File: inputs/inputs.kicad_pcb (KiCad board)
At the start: 2 copper layers, 47 x 25.4 mm, 27 parts, among them P1 CONN_01X01, P10 CONN_01X01, P11 CONN_01X01, P12 CONN_01X01, P13 CONN_01X01, P2 CONN_01X01, P3 CONN_01X01, P4 CONN_01X05, P5 CONN_01X01, P6 CONN_01X01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

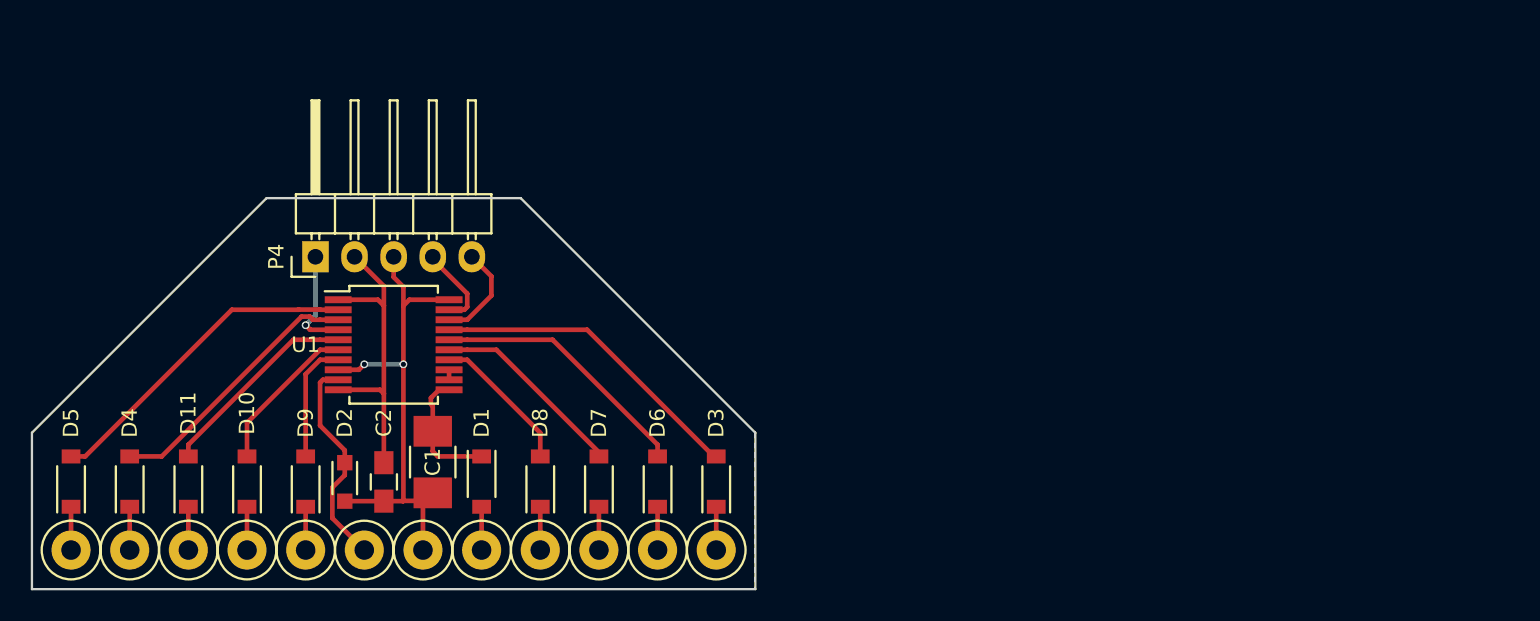
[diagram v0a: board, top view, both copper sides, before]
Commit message: 8 inputs rev 2
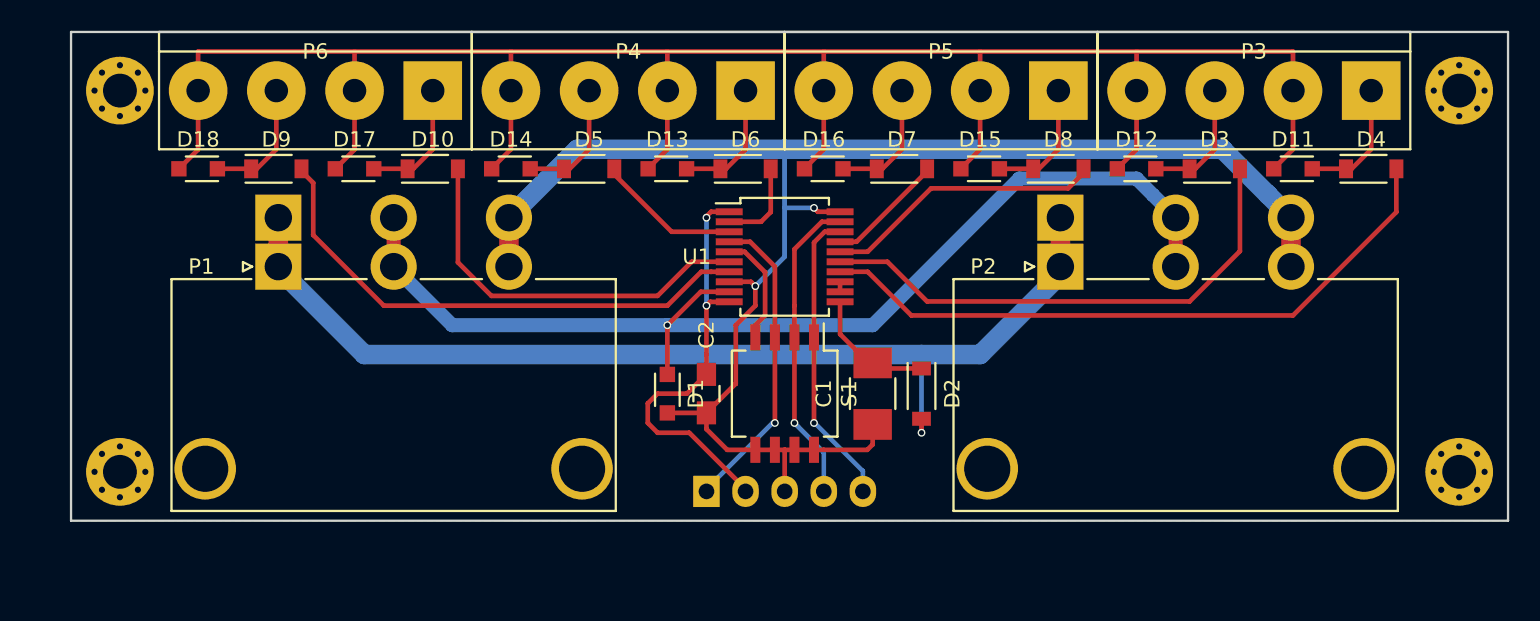
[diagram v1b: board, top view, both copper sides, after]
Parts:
- removed P10, P11, P12, P13, P8, P9: CONN_01X01, footprints:wire_awg_18
- added D12: RSB36V, Diodes_SMD:SOD-323_HandSoldering, F.Cu at (217.8, 64.8)
- added D13: RSB36V, Diodes_SMD:SOD-323_HandSoldering, F.Cu at (187.3, 64.8)
- added D14: RSB36V, Diodes_SMD:SOD-323_HandSoldering, F.Cu at (177.2, 64.8)
- added D15: RSB36V, Diodes_SMD:SOD-323_HandSoldering, F.Cu at (207.6, 64.8)
- added D16: RSB36V, Diodes_SMD:SOD-323_HandSoldering, F.Cu at (197.5, 64.8)
- added D17: RSB36V, Diodes_SMD:SOD-323_HandSoldering, F.Cu at (167.0, 64.8)
- added D18: RSB36V, Diodes_SMD:SOD-323_HandSoldering, F.Cu at (156.8, 64.8)
- added REF**: MountingHole_2.2mm_M2_Pad_Via, Mounting_Holes:MountingHole_2.2mm_M2_Pad_Via, F.Cu at (151.8, 84.5)
- added REF**: MountingHole_2.2mm_M2_Pad_Via, Mounting_Holes:MountingHole_2.2mm_M2_Pad_Via, F.Cu at (151.8, 59.7)
- added REF**: MountingHole_2.2mm_M2_Pad_Via, Mounting_Holes:MountingHole_2.2mm_M2_Pad_Via, F.Cu at (238.8, 59.7)
- added REF**: MountingHole_2.2mm_M2_Pad_Via, Mounting_Holes:MountingHole_2.2mm_M2_Pad_Via, F.Cu at (238.8, 84.5)
- added S1: DIP_SWITCH_4, footprints:Copal_CHS-04TB, F.Cu at (194.9, 79.4)
- D1, D11: value 1N4148W-7-F -> RSB36V; footprint Diodes_SMD:SOD-123 -> Diodes_SMD:SOD-323_HandSoldering
- D2: value RSB36V -> 1N4148W-7-F; footprint Diodes_SMD:SOD-323_HandSoldering -> Diodes_SMD:SOD-123
- P1, P2: value CONN_01X01 -> MOLEX-0431603103; footprint footprints:wire_awg_18 -> Connectors_Molex:Molex_Sabre_43160-XX03_03x7.49mm_Angled_BoardLock
- P3, P5, P6: value CONN_01X01 -> TE-282836-4; footprint footprints:wire_awg_18 -> Connect:bornier4
- P4: value CONN_01X05 -> TE-282836-4; footprint Pin_Headers:Pin_Header_Angled_1x05 -> Connect:bornier4
- P7: value CONN_01X01 -> CONN_01X05; footprint footprints:wire_awg_18 -> Pin_Headers:Pin_Header_Angled_1x05; moved to B.Cu
- moved D4 83.2 mm to (233.0, 64.8), turned to 0 degrees
- moved D11 74.6 mm to (228.0, 64.8), turned to 180 degrees
- moved P3 65.0 mm to (225.4, 59.7), turned to 180 degrees
- moved P2 45.3 mm to (212.9, 71.1)
- moved P7 41.5 mm to (189.9, 85.7), turned to 270 degrees
- moved D5 39.3 mm to (182.2, 64.8), turned to 0 degrees
- moved D8 39.3 mm to (212.7, 64.8), turned to 0 degrees
- moved D3 38.2 mm to (222.9, 64.8), turned to 0 degrees
- moved D2 37.9 mm to (203.8, 79.4)
- moved P5 33.2 mm to (205.1, 59.7), turned to 180 degrees
- moved P6 32.2 mm to (164.5, 59.7), turned to 180 degrees
- moved C1 28.9 mm to (200.7, 79.4)
- moved D7 28.3 mm to (202.6, 64.8), turned to 0 degrees
- moved U1 26.0 mm to (194.9, 70.5)
- moved D10 23.6 mm to (172.1, 64.8), turned to 0 degrees
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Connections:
- net Net-(D10-Pad2) renamed /Sheet584D84B8/CHAN_A
- net Net-(D9-Pad2) renamed /Sheet584D84B8/CHAN_B
- C1 pad 1: +12V -> /Sheet584DA639/+12V
- C2 pad 1: +5V -> /Sheet584DA639/+5V
- D1 pad 1: +12V -> /Sheet584DA639/LBUS
- D1 pad 2: Net-(D1-Pad2) -> GND
- D11 pad 2: Net-(D11-Pad2) -> GND
- D2 pad 1: /LBUS -> /Sheet584DA639/+12V
- D2 pad 2: GND -> /lin_common/12V_UNPROTECTED
- D3 pad 1: Net-(D3-Pad1) -> Net-(D12-Pad1)
- D3 pad 2: Net-(D3-Pad2) -> /Sheet584D6B96/CHAN_B
- D4 pad 1: Net-(D4-Pad1) -> Net-(D11-Pad1)
- D4 pad 2: Net-(D4-Pad2) -> /Sheet584D6B96/CHAN_A
- D5 pad 1: Net-(D5-Pad1) -> Net-(D14-Pad1)
- D5 pad 2: Net-(D5-Pad2) -> /Sheet584D7AB5/CHAN_B
- D6 pad 1: Net-(D6-Pad1) -> Net-(D13-Pad1)
- D6 pad 2: Net-(D6-Pad2) -> /Sheet584D7AB5/CHAN_A
- D7 pad 1: Net-(D7-Pad1) -> Net-(D16-Pad1)
- D7 pad 2: Net-(D7-Pad2) -> /Sheet584D8209/CHAN_B
- D8 pad 1: Net-(D8-Pad1) -> Net-(D15-Pad1)
- D8 pad 2: Net-(D8-Pad2) -> /Sheet584D8209/CHAN_A
- D9 pad 1: Net-(D9-Pad1) -> Net-(D18-Pad1)
- P1 pad 1: Net-(D1-Pad2) -> /lin_common/12V_UNPROTECTED
- P2 pad 1: GND -> /lin_common/12V_UNPROTECTED
- P3 pad 1: /LBUS -> Net-(D11-Pad1)
- P4 pad 1: //MCLR -> Net-(D13-Pad1)
- P4 pad 2: +5V -> GND
- P4 pad 3: GND -> Net-(D14-Pad1)
- P4 pad 4: /ICSPDAT -> GND
- P5 pad 1: Net-(D3-Pad1) -> Net-(D15-Pad1)
- P6 pad 1: Net-(D4-Pad1) -> Net-(D10-Pad1)
- P7 pad 1: Net-(D5-Pad1) -> /lin_common/A2
- U1 pad 1: +5V -> /Sheet584DA639/+5V
- U1 pad 10: +5V -> /Sheet584DA639/+5V
- U1 pad 11: +12V -> /Sheet584DA639/+12V
- U1 pad 14: Net-(D8-Pad2) -> /Sheet584D6B96/CHAN_A
- U1 pad 15: Net-(D7-Pad2) -> /Sheet584D6B96/CHAN_B
- U1 pad 16: Net-(D6-Pad2) -> /Sheet584D8209/CHAN_A
- U1 pad 17: Net-(D3-Pad2) -> /Sheet584D8209/CHAN_B
- U1 pad 18: /ICSPCLK -> /lin_common/A0
- U1 pad 19: /ICSPDAT -> /lin_common/A1
- U1 pad 2: Net-(D5-Pad2) -> /Sheet584D7AB5/CHAN_A
- U1 pad 3: Net-(D4-Pad2) -> /Sheet584D7AB5/CHAN_B
- U1 pad 4: //MCLR -> /lin_common/A2
- U1 pad 5: Net-(D11-Pad2) -> /lin_common/A3
- U1 pad 9: /LBUS -> /Sheet584DA639/LBUS
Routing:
- net GND: track 33.5 -> 241.0 mm
- net /Sheet584DA639/LBUS: track 0.00 -> 71.8 mm, vias 0 -> 1
- net /lin_common/12V_UNPROTECTED: track 0.00 -> 68.2 mm, vias 0 -> 1
- net /Sheet584D6B96/CHAN_A: track 0.00 -> 42.9 mm
- net /Sheet584D6B96/CHAN_B: track 0.00 -> 33.7 mm
- net /Sheet584DA639/+5V: track 0.00 -> 27.6 mm, vias 0 -> 2
- net /Sheet584D84B8/CHAN_B: track 7.85 -> 34.5 mm
- net Net-(D5-Pad2): track 21.3 -> 0.00 mm
- net Net-(D3-Pad2): track 20.8 -> 0.00 mm
- net +5V: track 20.4 -> 0.00 mm
- net /lin_common/A1: track 0.00 -> 20.2 mm, vias 0 -> 1
- net /lin_common/A2: track 0.00 -> 20.2 mm, vias 0 -> 1
- net /lin_common/A0: track 0.00 -> 19.5 mm, vias 0 -> 1
- net /Sheet584D8209/CHAN_A: track 0.00 -> 18.2 mm
- net Net-(D4-Pad2): track 17.4 -> 0.00 mm
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- removed copper zone on F.Cu, net GND
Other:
- board size 47 x 25.4 mm -> 93.3 x 31.7 mm
- board text added: "0"
- board text added: "8 inputs LIN module rev 2 Dec 2016 Cedric Priscal"
- board text removed: "8"
- board text removed: "9"
- board text removed: "9 inputs LIN module rev 1 11 Oct 2016 Cedric Priscal"
